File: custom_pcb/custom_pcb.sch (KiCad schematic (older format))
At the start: 284 parts, among them J1 USB_mini_micro_B, K0 KEYSW, K1 KEYSW, K10 KEYSW, K11 KEYSW, K12 KEYSW, K13 KEYSW, K14 KEYSW, K15 KEYSW, K16 KEYSW, K17 KEYSW, K18 KEYSW, K19 KEYSW, K2 KEYSW, K20 KEYSW, K21 KEYSW, K22 KEYSW, K23 KEYSW, K24 KEYSW, K25 KEYSW, K26 KEYSW, K27 KEYSW, K28 KEYSW, K29 KEYSW, K3 KEYSW, K30 KEYSW, K31 KEYSW, K32 KEYSW, K33 KEYSW, K34 KEYSW, K35 KEYSW, K36 KEYSW, K37 KEYSW, K38 KEYSW, K39 KEYSW, K4 KEYSW, K40 KEYSW, K41 KEYSW, K42 KEYSW, K43 KEYSW, K44 KEYSW, K45 KEYSW, K46 KEYSW, K47 KEYSW, K48 KEYSW, K49 KEYSW, K5 KEYSW, K50 KEYSW, K51 KEYSW, K52 KEYSW, K53 KEYSW, K54 KEYSW, K55 KEYSW, K56 KEYSW, K57 KEYSW, K58 KEYSW, K59 KEYSW, K6 KEYSW, K60 KEYSW, K61 KEYSW, K62 KEYSW, K63 KEYSW, K64 KEYSW, K65 KEYSW, K66 KEYSW, K67 KEYSW, K68 KEYSW, K69 KEYSW, K7 KEYSW, K70 KEYSW, K71 KEYSW, K72 KEYSW, K73 KEYSW, K74 KEYSW, K75 KEYSW, K76 KEYSW, K77 KEYSW, K78 KEYSW, K79 KEYSW, K8 KEYSW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

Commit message: started work on ground planes and rerouting the led tracks so that the via is on the anode saving 4 vias per led
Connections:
- net labels added: VCC
- wire segments 460 -> 471
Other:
- moved on the sheet: J1, U2
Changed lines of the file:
@@
 L MKL02Z32VFG4 U2
 U 1 1 5892E040
-P 5400 1200
-F 0 "U2" H 4300 1750 50  0000 L CNN
-F 1 "MKL02Z32VFG4" H 4300 600 50  0000 L CNN
-F 2 "MKL02Z32VFG4:QFN50P300X300X65-17N" H 5400 1200 50  0001 L CNN
-F 3 "MKL02Z32VFG4" H 5400 1200 50  0001 L CNN
-F 4 "QFN-16 NXP Semiconductors" H 5400 1200 50  0001 L CNN "Package"
-F 5 "NXP Semiconductors" H 5400 1200 50  0001 L CNN "MF"
-F 6 "1.33 USD" H 5400 1200 50  0001 L CNN "Price"
-F 7 "32 Bit Microcontroller, Kinetis L Series Ultra Low Power, ARM Cortex-M0+, 48 MHz, 32 KB, 4 KB, 16" H 5400 1200 50  0001 L CNN "Description"
-F 8 "Good" H 5400 1200 50  0001 L CNN "Availability"
-	1    5400 1200
+P 6000 1250
+F 0 "U2" H 4900 1800 50  0000 L CNN
+F 1 "MKL02Z32VFG4" H 4900 650 50  0000 L CNN
+F 2 "MKL02Z32VFG4:QFN50P300X300X65-17N" H 6000 1250 50  0001 L CNN
+F 3 "MKL02Z32VFG4" H 6000 1250 50  0001 L CNN
+F 4 "QFN-16 NXP Semiconductors" H 6000 1250 50  0001 L CNN "Package"
+F 5 "NXP Semiconductors" H 6000 1250 50  0001 L CNN "MF"
+F 6 "1.33 USD" H 6000 1250 50  0001 L CNN "Price"
+F 7 "32 Bit Microcontroller, Kinetis L Series Ultra Low Power, ARM Cortex-M0+, 48 MHz, 32 KB, 4 KB, 16" H 6000 1250 50  0001 L CNN "Description"
+F 8 "Good" H 6000 1250 50  0001 L CNN "Availability"
+	1    6000 1250
 	1    0    0    -1
 $EndComp
@@
 L USB_mini_micro_B J1
 U 1 1 589DEC60
-P 3950 1000
-F 0 "J1" H 3550 950 60  0000 C CNN
-F 1 "USB_mini_micro_B" H 3800 1250 60  0001 C CNN
-F 2 "keyboard_parts:USB_miniB_hirose_5S8" H 3900 1000 60  0001 C CNN
-F 3 "" H 3900 1000 60  0000 C CNN
-	1    3950 1000
+P 4250 1000
+F 0 "J1" H 3850 950 60  0000 C CNN
+F 1 "USB_mini_micro_B" H 4100 1250 60  0001 C CNN
+F 2 "keyboard_parts:USB_miniB_hirose_5S8" H 4200 1000 60  0001 C CNN
+F 3 "" H 4200 1000 60  0000 C CNN
+	1    4250 1000
 	0    1    1    0
 $EndComp
@@
 Text GLabel 1050 1850 0    60   Input ~ 0
 TP_CLK
-Text GLabel 4500 2500 1    60   Input ~ 0
-GND
 Text GLabel 4200 2500 1    60   Input ~ 0
 TP_DATA
@@
 Text GLabel 4500 3650 2    60   Input ~ 0
 BTN2
-Text GLabel 3350 1950 2    60   Input ~ 0
-GND
 Text Notes 3650 4150 0    60   ~ 0
 Note that when wiring the LVC9 -> mainboard \nconnector the BTN0 and BTN2 leads need to be\nswapped since the order is reversed here to simplify routing.
-Text GLabel 3900 3050 0    60   Input ~ 0
-GND
-Text GLabel 3900 3350 0    60   Input ~ 0
-GND
-Text GLabel 3900 3650 0    60   Input ~ 0
-GND
 Text GLabel 8600 8000 0    60   Input ~ 0
 LED_DATA0
@@
 Text GLabel 1050 3550 0    60   Input ~ 0
 TP_RST
-Text GLabel 8600 7900 0    60   Input ~ 0
-GND
-Text GLabel 11250 7900 0    60   Input ~ 0
-GND
-Text GLabel 13200 7900 0    60   Input ~ 0
-GND
+Text GLabel 9750 7900 2    60   Input ~ 0
+V3.3
+Text GLabel 12400 7900 2    60   Input ~ 0
+V3.3
+Text GLabel 14350 7900 2    60   Input ~ 0
+V3.3
+Text GLabel 3350 850  2    60   Input ~ 0
+V3.3
+Text GLabel 4400 1150 3    60   Input ~ 0
+VCC
+$Comp
+L GND #PWR01
+U 1 1 589EB648
+P 4000 1250
+F 0 "#PWR01" H 4000 1000 50  0001 C CNN
+F 1 "GND" H 4000 1100 50  0000 C CNN
+F 2 "" H 4000 1250 50  0000 C CNN
+F 3 "" H 4000 1250 50  0000 C CNN
+	1    4000 1250
+	1    0    0    -1
+$EndComp
+$Comp
+L GND #PWR02
+U 1 1 589ED4FE
+P 3350 2250
+F 0 "#PWR02" H 3350 2000 50  0001 C CNN
+F 1 "GND" H 3350 2100 50  0000 C CNN
+F 2 "" H 3350 2250 50  0000 C CNN
+F 3 "" H 3350 2250 50  0000 C CNN
+	1    3350 2250
+	1    0    0    -1
+$EndComp
+$Comp
+L GND #PWR03
+U 1 1 589EDA95
+P 4700 2500
+F 0 "#PWR03" H 4700 2250 50  0001 C CNN
+F 1 "GND" H 4700 2350 50  0000 C CNN
+F 2 "" H 4700 2500 50  0000 C CNN
+F 3 "" H 4700 2500 50  0000 C CNN
+	1    4700 2500
+	1    0    0    -1
+$EndComp
 Connection ~ 7950 9850
 Connection ~ 7450 9850
@@
 Connection ~ 8200 1800
 Connection ~ 8200 2200
-Text GLabel 9750 7900 2    60   Input ~ 0
-V3.3
-Text GLabel 12400 7900 2    60   Input ~ 0
-V3.3
-Text GLabel 14350 7900 2    60   Input ~ 0
-V3.3
+Wire Wire Line
+	4000 1150 4000 1250
+Wire Wire Line
+	4500 2500 4700 2500
+$Comp
+L GND #PWR04
+U 1 1 589F0C49
+P 3900 3050
+F 0 "#PWR04" H 3900 2800 50  0001 C CNN
+F 1 "GND" H 3900 2900 50  0000 C CNN
+F 2 "" H 3900 3050 50  0000 C CNN
+F 3 "" H 3900 3050 50  0000 C CNN
+	1    3900 3050
+	1    0    0    -1
+$EndComp
+$Comp
+L GND #PWR05
+U 1 1 589F1F30
+P 3900 3350
+F 0 "#PWR05" H 3900 3100 50  0001 C CNN
+F 1 "GND" H 3900 3200 50  0000 C CNN
+F 2 "" H 3900 3350 50  0000 C CNN
+F 3 "" H 3900 3350 50  0000 C CNN
+	1    3900 3350
+	1    0    0    -1
+$EndComp
+$Comp
+L GND #PWR06
+U 1 1 589F2A53
+P 3900 3650
+F 0 "#PWR06" H 3900 3400 50  0001 C CNN
+F 1 "GND" H 3900 3500 50  0000 C CNN
+F 2 "" H 3900 3650 50  0000 C CNN
+F 3 "" H 3900 3650 50  0000 C CNN
+	1    3900 3650
+	1    0    0    -1
+$EndComp
+$Comp
+L GND #PWR07
+U 1 1 589F4307
+P 8450 7650
+F 0 "#PWR07" H 8450 7400 50  0001 C CNN
+F 1 "GND" H 8450 7500 50  0000 C CNN
+F 2 "" H 8450 7650 50  0000 C CNN
+F 3 "" H 8450 7650 50  0000 C CNN
+	1    8450 7650
+	1    0    0    -1
+$EndComp
+Wire Wire Line
+	8600 7900 8600 7650
+Wire Wire Line
+	8600 7650 8450 7650
+$Comp
+L GND #PWR08
+U 1 1 589F720F
+P 11000 7750
+F 0 "#PWR08" H 11000 7500 50  0001 C CNN
+F 1 "GND" H 11000 7600 50  0000 C CNN
+F 2 "" H 11000 7750 50  0000 C CNN
+F 3 "" H 11000 7750 50  0000 C CNN
+	1    11000 7750
+	1    0    0    -1
+$EndComp
+$Comp
+L GND #PWR09
+U 1 1 589F7E4E
+P 12850 7750
+F 0 "#PWR09" H 12850 7500 50  0001 C CNN
+F 1 "GND" H 12850 7600 50  0000 C CNN
+F 2 "" H 12850 7750 50  0000 C CNN
+F 3 "" H 12850 7750 50  0000 C CNN
+	1    12850 7750
+	1    0    0    -1
+$EndComp
+Wire Wire Line
+	13200 7900 13000 7900
+Wire Wire Line
+	13000 7900 13000 7750
+Wire Wire Line
+	13000 7750 12850 7750
+Wire Wire Line
+	11250 7900 11250 7750
+Wire Wire Line
+	11250 7750 11000 7750
+$Comp
+L GND #PWR?
+U 1 1 58A0FDAB
+P 3800 1200
+F 0 "#PWR?" H 3800 950 50  0001 C CNN
+F 1 "GND" H 3800 1050 50  0000 C CNN
+F 2 "" H 3800 1200 50  0000 C CNN
+F 3 "" H 3800 1200 50  0000 C CNN
+	1    3800 1200
+	1    0    0    -1
+$EndComp
+Wire Wire Line
+	3900 1150 3800 1150
+Wire Wire Line
+	3800 1150 3800 1200
 $EndSCHEMATC

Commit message: sch rewiring for leds
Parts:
- added R10, R11, R12, R7, R8, R9: R, Resistors_SMD:R_0402, symbol R
- SMD_LED10, SMD_LED100, SMD_LED101, SMD_LED102, SMD_LED103, SMD_LED104, SMD_LED11, SMD_LED12, SMD_LED13, SMD_LED15, SMD_LED16, SMD_LED17, SMD_LED18, SMD_LED19, SMD_LED20, SMD_LED21, SMD_LED22, SMD_LED23, SMD_LED24, SMD_LED25, SMD_LED26, SMD_LED27, SMD_LED28, SMD_LED30, SMD_LED31, SMD_LED32, SMD_LED33, SMD_LED34, SMD_LED35, SMD_LED36, SMD_LED37, SMD_LED38, SMD_LED39, SMD_LED40, SMD_LED41, SMD_LED42, SMD_LED43, SMD_LED45, SMD_LED46, SMD_LED47, SMD_LED48, SMD_LED49, SMD_LED50, SMD_LED51, SMD_LED52, SMD_LED53, SMD_LED54, SMD_LED55, SMD_LED56, SMD_LED57, SMD_LED58, SMD_LED60, SMD_LED61, SMD_LED62, SMD_LED63, SMD_LED64, SMD_LED65, SMD_LED66, SMD_LED67, SMD_LED68, SMD_LED69, SMD_LED7, SMD_LED70, SMD_LED71, SMD_LED72, SMD_LED75, SMD_LED76, SMD_LED77, SMD_LED78, SMD_LED79, SMD_LED8, SMD_LED80, SMD_LED81, SMD_LED82, SMD_LED83, SMD_LED84, SMD_LED85, SMD_LED86, SMD_LED87, SMD_LED88, SMD_LED89, SMD_LED9, SMD_LED90, SMD_LED91, SMD_LED92, SMD_LED93, SMD_LED94, SMD_LED95, SMD_LED96, SMD_LED97, SMD_LED98, SMD_LED99: footprint cherry_rgb:SMLVN6RGB -> cherry_rgb:SMLVN6RGB_CA
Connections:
- net labels added: blue10, blue11, blue12, blue7, blue8, blue9, green10, green11, green12, green7, green8, green9, red10, red11, red12, red7, red8, red9
- net labels removed: anode10, anode11, anode12, anode13, anode14, anode7, anode8, anode9
- wire segments 471 -> 1727
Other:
- moved on the sheet: R0, R1, R2, R3, R4, R5, R6

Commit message: cpcb good timepoint
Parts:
- SMD_LED10, SMD_LED100, SMD_LED101, SMD_LED102, SMD_LED103, SMD_LED104, SMD_LED11, SMD_LED12, SMD_LED13, SMD_LED15, SMD_LED16, SMD_LED17, SMD_LED18, SMD_LED19, SMD_LED20, SMD_LED21, SMD_LED22, SMD_LED23, SMD_LED24, SMD_LED25, SMD_LED26, SMD_LED27, SMD_LED28, SMD_LED30, SMD_LED31, SMD_LED32, SMD_LED33, SMD_LED34, SMD_LED35, SMD_LED36, SMD_LED37, SMD_LED38, SMD_LED39, SMD_LED40, SMD_LED41, SMD_LED42, SMD_LED43, SMD_LED45, SMD_LED46, SMD_LED47, SMD_LED48, SMD_LED49, SMD_LED50, SMD_LED51, SMD_LED52, SMD_LED53, SMD_LED54, SMD_LED55, SMD_LED56, SMD_LED57, SMD_LED58, SMD_LED60, SMD_LED61, SMD_LED62, SMD_LED63, SMD_LED64, SMD_LED65, SMD_LED66, SMD_LED67, SMD_LED68, SMD_LED69, SMD_LED7, SMD_LED70, SMD_LED71, SMD_LED72, SMD_LED75, SMD_LED76, SMD_LED77, SMD_LED78, SMD_LED79, SMD_LED8, SMD_LED80, SMD_LED81, SMD_LED82, SMD_LED83, SMD_LED84, SMD_LED85, SMD_LED86, SMD_LED87, SMD_LED88, SMD_LED89, SMD_LED9, SMD_LED90, SMD_LED91, SMD_LED92, SMD_LED93, SMD_LED94, SMD_LED95, SMD_LED96, SMD_LED97, SMD_LED98, SMD_LED99: value SMLVN6RGB -> SMLVN6RGB_CA; symbol SMLVN6RGB -> SMLVN6RGB_CA
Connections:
- wire segments 1727 -> 3410

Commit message: cpcb actually good timepoint
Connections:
- wire segments 3410 -> 2488

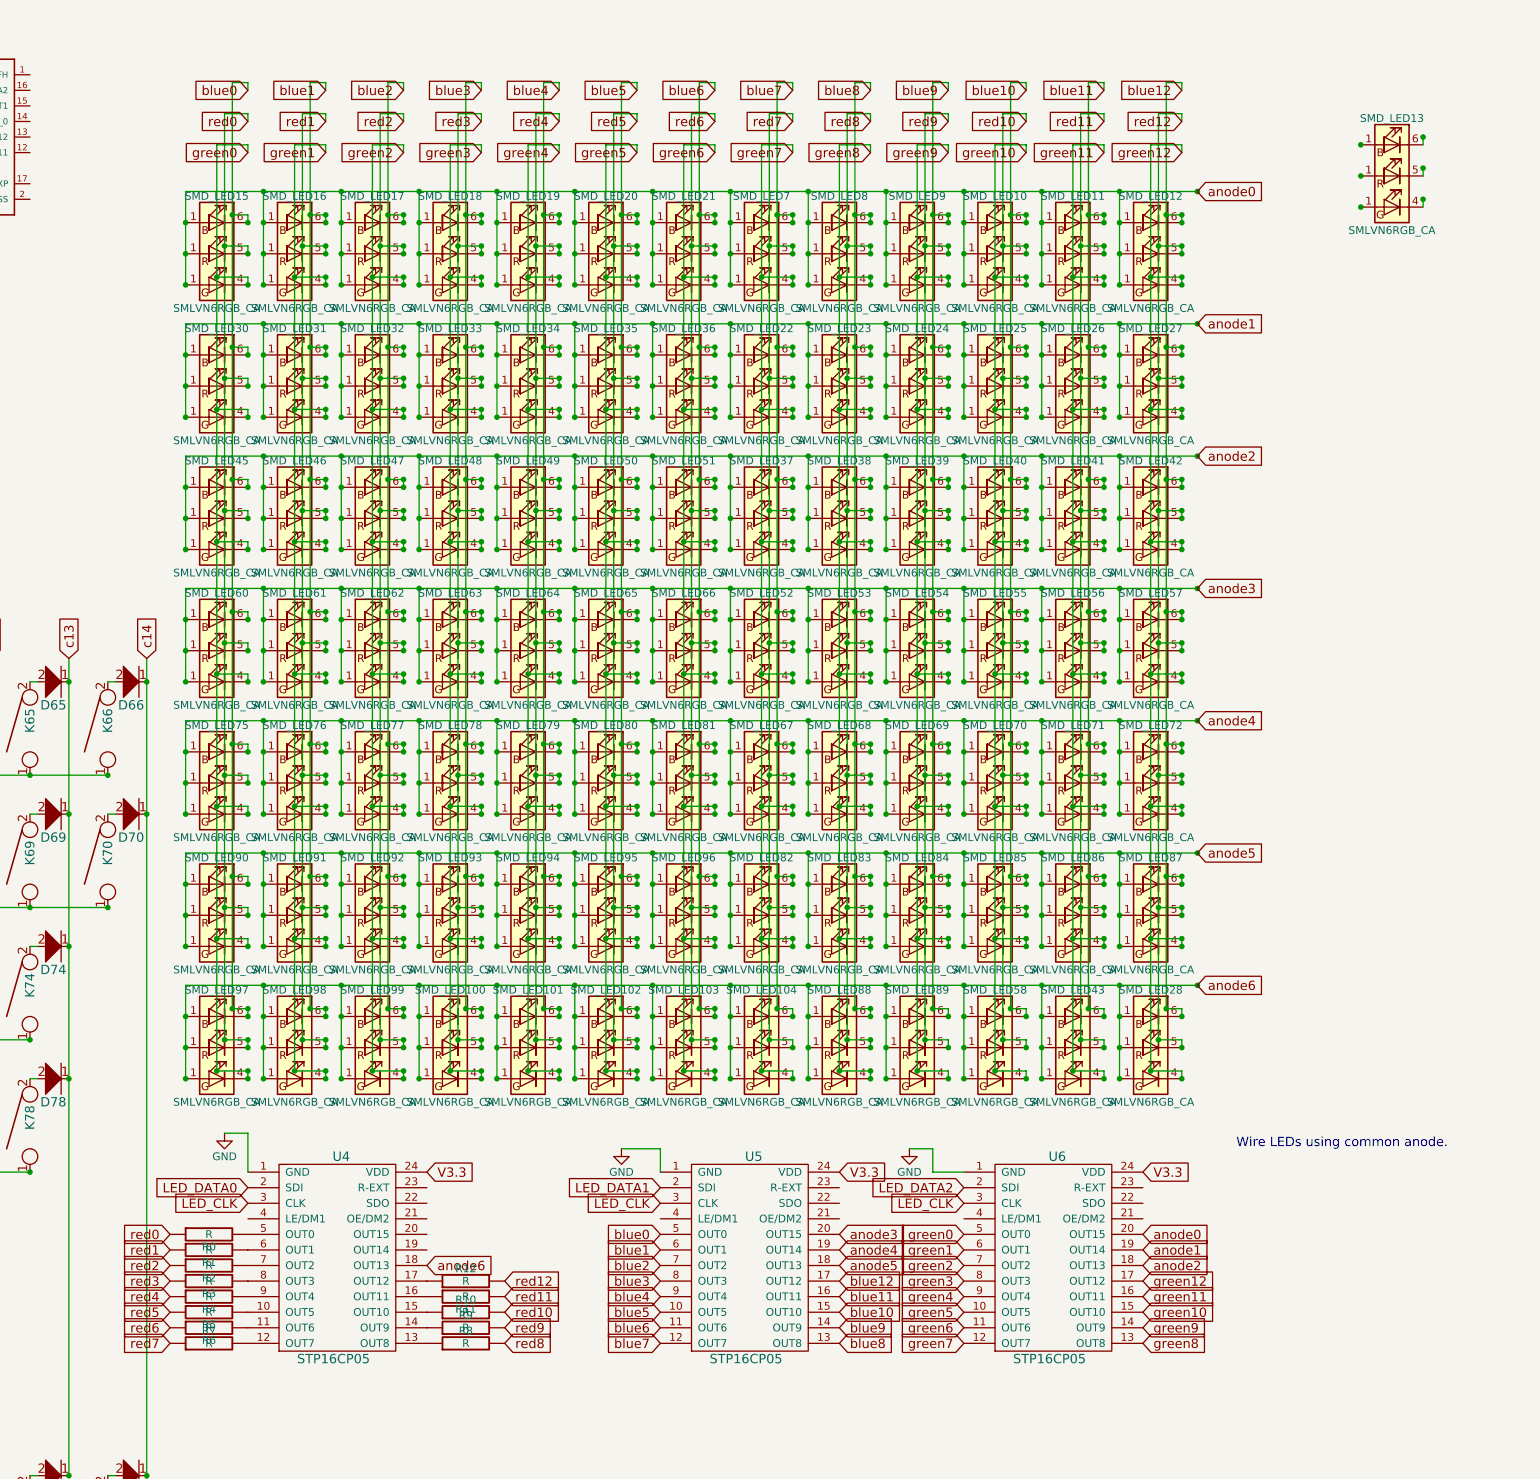
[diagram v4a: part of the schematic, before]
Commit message: cpcb lots more relestate down at the bottom for the control circuitry
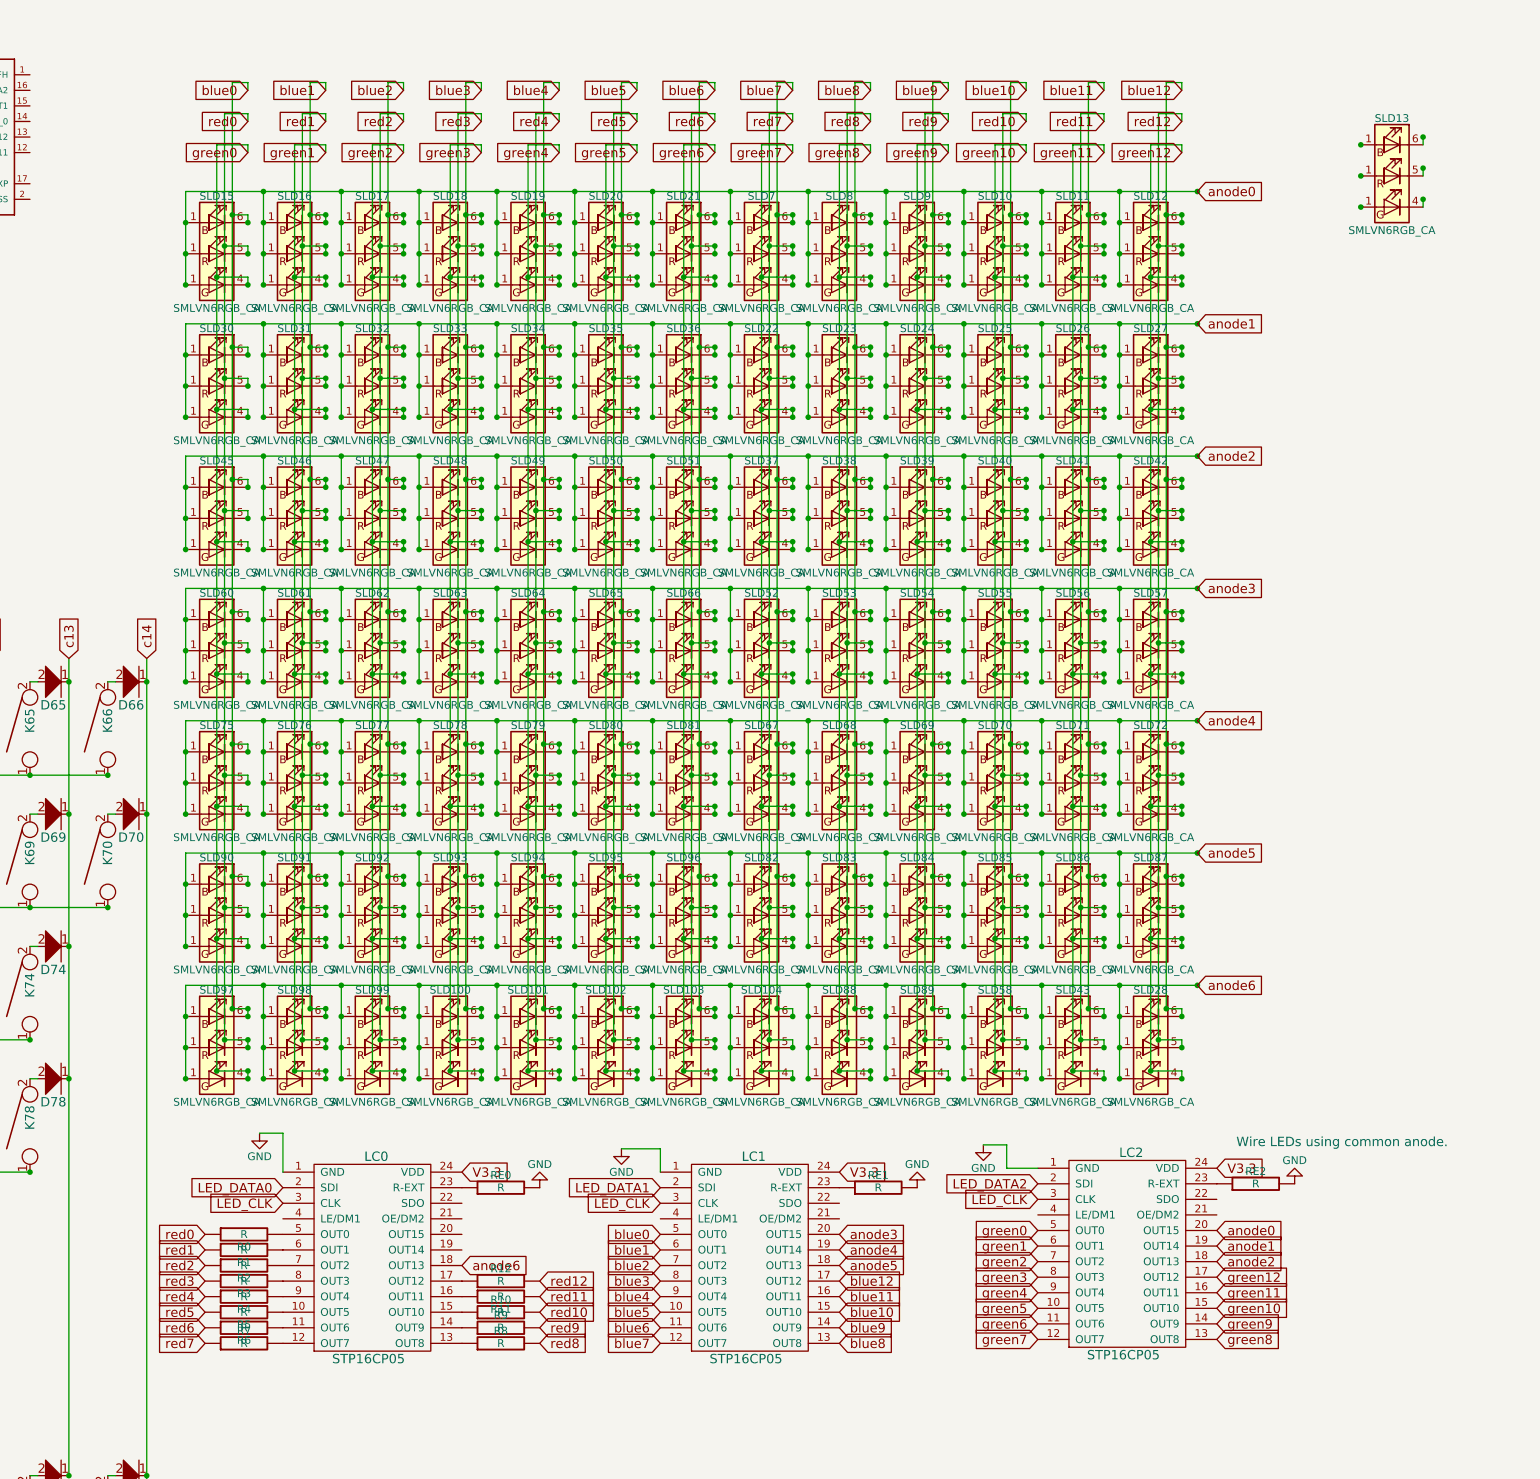
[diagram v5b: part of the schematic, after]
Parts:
- added RE0, RE1, RE2: R, Resistors_SMD:R_0603_HandSoldering, symbol R
- K0, K64: footprint cherry_rgb:CHERRY_PLATE_150V -> cherry_rgb:CHERRY_PLATE_200V
- MOUSE0, MOUSE2: footprint cherry_rgb:CHERRY_PLATE_175H -> cherry_rgb:CHERRY_PLATE_150H
- R0, R1, R10, R11, R12, R2, R3, R4, R5, R6, R7, R8, R9: footprint Resistors_SMD:R_0402 -> Resistors_SMD:R_0603_HandSoldering
- renumbered U4 to LC0, U5 to LC1, U6 to LC2, SMD_LED10 to SLD10, SMD_LED100 to SLD100, SMD_LED101 to SLD101, SMD_LED102 to SLD102, SMD_LED103 to SLD103, SMD_LED104 to SLD104, SMD_LED11 to SLD11, SMD_LED12 to SLD12, SMD_LED13 to SLD13, SMD_LED15 to SLD15, SMD_LED16 to SLD16, SMD_LED17 to SLD17, SMD_LED18 to SLD18, SMD_LED19 to SLD19, SMD_LED20 to SLD20, SMD_LED21 to SLD21, SMD_LED22 to SLD22, SMD_LED23 to SLD23, SMD_LED24 to SLD24, SMD_LED25 to SLD25, SMD_LED26 to SLD26, SMD_LED27 to SLD27, SMD_LED28 to SLD28, SMD_LED30 to SLD30, SMD_LED31 to SLD31, SMD_LED32 to SLD32, SMD_LED33 to SLD33, SMD_LED34 to SLD34, SMD_LED35 to SLD35, SMD_LED36 to SLD36, SMD_LED37 to SLD37, SMD_LED38 to SLD38, SMD_LED39 to SLD39, SMD_LED40 to SLD40, SMD_LED41 to SLD41, SMD_LED42 to SLD42, SMD_LED43 to SLD43, SMD_LED45 to SLD45, SMD_LED46 to SLD46, SMD_LED47 to SLD47, SMD_LED48 to SLD48, SMD_LED49 to SLD49, SMD_LED50 to SLD50, SMD_LED51 to SLD51, SMD_LED52 to SLD52, SMD_LED53 to SLD53, SMD_LED54 to SLD54, SMD_LED55 to SLD55, SMD_LED56 to SLD56, SMD_LED57 to SLD57, SMD_LED58 to SLD58, SMD_LED60 to SLD60, SMD_LED61 to SLD61, SMD_LED62 to SLD62, SMD_LED63 to SLD63, SMD_LED64 to SLD64, SMD_LED65 to SLD65, SMD_LED66 to SLD66, SMD_LED67 to SLD67, SMD_LED68 to SLD68, SMD_LED69 to SLD69, SMD_LED7 to SLD7, SMD_LED70 to SLD70, SMD_LED71 to SLD71, SMD_LED72 to SLD72, SMD_LED75 to SLD75, SMD_LED76 to SLD76, SMD_LED77 to SLD77, SMD_LED78 to SLD78, SMD_LED79 to SLD79, SMD_LED8 to SLD8, SMD_LED80 to SLD80, SMD_LED81 to SLD81, SMD_LED82 to SLD82, SMD_LED83 to SLD83, SMD_LED84 to SLD84, SMD_LED85 to SLD85, SMD_LED86 to SLD86, SMD_LED87 to SLD87, SMD_LED88 to SLD88, SMD_LED89 to SLD89, SMD_LED9 to SLD9, SMD_LED90 to SLD90, SMD_LED91 to SLD91, SMD_LED92 to SLD92, SMD_LED93 to SLD93, SMD_LED94 to SLD94, SMD_LED95 to SLD95, SMD_LED96 to SLD96, SMD_LED97 to SLD97, SMD_LED98 to SLD98, SMD_LED99 to SLD99
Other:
- moved on the sheet: LC0, LC2, R0, R1, R10, R11, R12, R2, R3, R4, R5, R6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

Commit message: cpcb sch small changes?
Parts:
- R0, R1, R10, R11, R12, R2, R3, R4, R5, R6, R7, R8, R9: footprint Resistors_SMD:R_0603_HandSoldering -> Resistors_SMD:R_0402_NoSilk
- RE0, RE1, RE2: footprint Resistors_SMD:R_0603_HandSoldering -> Resistors_SMD:R_0402
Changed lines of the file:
@@
 F 0 "R6" V 8655 8900 50  0000 C CNN
 F 1 "R" V 8575 8900 50  0000 C CNN
-F 2 "Resistors_SMD:R_0603_HandSoldering" H 8575 8900 60  0001 C CNN
+F 2 "Resistors_SMD:R_0402_NoSilk" H 8575 8900 60  0001 C CNN
 F 3 "" H 8575 8900 60  0000 C CNN
 	1    8575 8900
@@
 F 0 "R5" V 8655 8800 50  0000 C CNN
 F 1 "R" V 8575 8800 50  0000 C CNN
-F 2 "Resistors_SMD:R_0603_HandSoldering" H 8575 8800 60  0001 C CNN
+F 2 "Resistors_SMD:R_0402_NoSilk" H 8575 8800 60  0001 C CNN
 F 3 "" H 8575 8800 60  0000 C CNN
 	1    8575 8800
@@
 F 0 "R4" V 8655 8700 50  0000 C CNN
 F 1 "R" V 8575 8700 50  0000 C CNN
-F 2 "Resistors_SMD:R_0603_HandSoldering" H 8575 8700 60  0001 C CNN
+F 2 "Resistors_SMD:R_0402_NoSilk" H 8575 8700 60  0001 C CNN
 F 3 "" H 8575 8700 60  0000 C CNN
 	1    8575 8700
@@
 F 0 "R3" V 8655 8600 50  0000 C CNN
 F 1 "R" V 8575 8600 50  0000 C CNN
-F 2 "Resistors_SMD:R_0603_HandSoldering" H 8575 8600 60  0001 C CNN
+F 2 "Resistors_SMD:R_0402_NoSilk" H 8575 8600 60  0001 C CNN
 F 3 "" H 8575 8600 60  0000 C CNN
 	1    8575 8600
@@
 F 0 "R2" V 8655 8500 50  0000 C CNN
 F 1 "R" V 8575 8500 50  0000 C CNN
-F 2 "Resistors_SMD:R_0603_HandSoldering" H 8575 8500 60  0001 C CNN
+F 2 "Resistors_SMD:R_0402_NoSilk" H 8575 8500 60  0001 C CNN
 F 3 "" H 8575 8500 60  0000 C CNN
 	1    8575 8500
@@
 F 0 "R1" V 8655 8400 50  0000 C CNN
 F 1 "R" V 8575 8400 50  0000 C CNN
-F 2 "Resistors_SMD:R_0603_HandSoldering" H 8575 8400 60  0001 C CNN
+F 2 "Resistors_SMD:R_0402_NoSilk" H 8575 8400 60  0001 C CNN
 F 3 "" H 8575 8400 60  0000 C CNN
 	1    8575 8400
@@
 F 0 "R0" V 8655 8300 50  0000 C CNN
 F 1 "R" V 8575 8300 50  0000 C CNN
-F 2 "Resistors_SMD:R_0603_HandSoldering" H 8575 8300 60  0001 C CNN
+F 2 "Resistors_SMD:R_0402_NoSilk" H 8575 8300 60  0001 C CNN
 F 3 "" H 8575 8300 60  0000 C CNN
 	1    8575 8300
@@
 F 0 "R12" V 10305 8600 50  0000 C CNN
 F 1 "R" V 10225 8600 50  0000 C CNN
-F 2 "Resistors_SMD:R_0603_HandSoldering" H 10225 8600 60  0001 C CNN
+F 2 "Resistors_SMD:R_0402_NoSilk" H 10225 8600 60  0001 C CNN
 F 3 "" H 10225 8600 60  0000 C CNN
 	1    10225 8600
@@
 F 0 "R10" V 10305 8800 50  0000 C CNN
 F 1 "R" V 10225 8800 50  0000 C CNN
-F 2 "Resistors_SMD:R_0603_HandSoldering" H 10225 8800 60  0001 C CNN
+F 2 "Resistors_SMD:R_0402_NoSilk" H 10225 8800 60  0001 C CNN
 F 3 "" H 10225 8800 60  0000 C CNN
 	1    10225 8800
@@
 F 0 "R9" V 10305 8900 50  0000 C CNN
 F 1 "R" V 10225 8900 50  0000 C CNN
-F 2 "Resistors_SMD:R_0603_HandSoldering" H 10225 8900 60  0001 C CNN
+F 2 "Resistors_SMD:R_0402_NoSilk" H 10225 8900 60  0001 C CNN
 F 3 "" H 10225 8900 60  0000 C CNN
 	1    10225 8900
@@
 F 0 "R8" V 10305 9000 50  0000 C CNN
 F 1 "R" V 10225 9000 50  0000 C CNN
-F 2 "Resistors_SMD:R_0603_HandSoldering" H 10225 9000 60  0001 C CNN
+F 2 "Resistors_SMD:R_0402_NoSilk" H 10225 9000 60  0001 C CNN
 F 3 "" H 10225 9000 60  0000 C CNN
 	1    10225 9000
@@
 F 0 "R7" V 8655 9000 50  0000 C CNN
 F 1 "R" V 8575 9000 50  0000 C CNN
-F 2 "Resistors_SMD:R_0603_HandSoldering" H 8575 9000 60  0001 C CNN
+F 2 "Resistors_SMD:R_0402_NoSilk" H 8575 9000 60  0001 C CNN
 F 3 "" H 8575 9000 60  0000 C CNN
 	1    8575 9000
@@
 F 0 "R11" V 10305 8700 50  0000 C CNN
 F 1 "R" V 10225 8700 50  0000 C CNN
-F 2 "Resistors_SMD:R_0603_HandSoldering" H 10225 8700 60  0001 C CNN
+F 2 "Resistors_SMD:R_0402_NoSilk" H 10225 8700 60  0001 C CNN
 F 3 "" H 10225 8700 60  0000 C CNN
 	1    10225 8700
@@
 F 0 "RE0" V 10305 8000 50  0000 C CNN
 F 1 "R" V 10225 8000 50  0000 C CNN
-F 2 "Resistors_SMD:R_0603_HandSoldering" H 10225 8000 60  0001 C CNN
+F 2 "Resistors_SMD:R_0402" H 10225 8000 60  0001 C CNN
 F 3 "" H 10225 8000 60  0000 C CNN
 	1    10225 8000
@@
 F 0 "RE1" V 12730 8000 50  0000 C CNN
 F 1 "R" V 12650 8000 50  0000 C CNN
-F 2 "Resistors_SMD:R_0603_HandSoldering" H 12650 8000 60  0001 C CNN
+F 2 "Resistors_SMD:R_0402" H 12650 8000 60  0001 C CNN
 F 3 "" H 12650 8000 60  0000 C CNN
 	1    12650 8000
@@
 F 0 "RE2" V 15155 7975 50  0000 C CNN
 F 1 "R" V 15075 7975 50  0000 C CNN
-F 2 "Resistors_SMD:R_0603_HandSoldering" H 15075 7975 60  0001 C CNN
+F 2 "Resistors_SMD:R_0402" H 15075 7975 60  0001 C CNN
 F 3 "" H 15075 7975 60  0000 C CNN
 	1    15075 7975
@@
 $EndComp
 $Comp
-L GND #PWR?
+L GND #PWR011
 U 1 1 58B5805D
 P 10475 8000
-F 0 "#PWR?" H 10475 7750 50  0001 C CNN
+F 0 "#PWR011" H 10475 7750 50  0001 C CNN
 F 1 "GND" H 10475 7850 50  0000 C CNN
 F 2 "" H 10475 8000 50  0000 C CNN
@@
 $EndComp
 $Comp
-L GND #PWR?
+L GND #PWR012
 U 1 1 58B583D7
 P 12900 8000
-F 0 "#PWR?" H 12900 7750 50  0001 C CNN
+F 0 "#PWR012" H 12900 7750 50  0001 C CNN
 F 1 "GND" H 12900 7850 50  0000 C CNN
 F 2 "" H 12900 8000 50  0000 C CNN
@@
 $EndComp
 $Comp
-L GND #PWR?
+L GND #PWR013
 U 1 1 58B59079
 P 15325 7975
-F 0 "#PWR?" H 15325 7725 50  0001 C CNN
+F 0 "#PWR013" H 15325 7725 50  0001 C CNN
 F 1 "GND" H 15325 7825 50  0000 C CNN
 F 2 "" H 15325 7975 50  0000 C CNN
